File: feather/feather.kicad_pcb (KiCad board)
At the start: 4 copper layers, 61.4 x 38.8 mm, 145 parts, among them CN1 ST-0337D00-071-1A2H, CN2 GT-3321667P-01, J1 Connector, USB-TYPE-C-16P, SW1 1TS015A-1400-0600-CT, SW2 1TS015A-1400-0600-CT, U1 TLV76733DRVx, U10 OPA1622, U11 OPA1622, U2 LM27762, U3 TAD5242IRGER, U4 TLV76733DRVx, U5 OPA1612AxD, U6 RP2350A-QFN60, U7 OPA1612AxD, U8 OPA1612AxD, U9 OPA1622, X1 12MHz

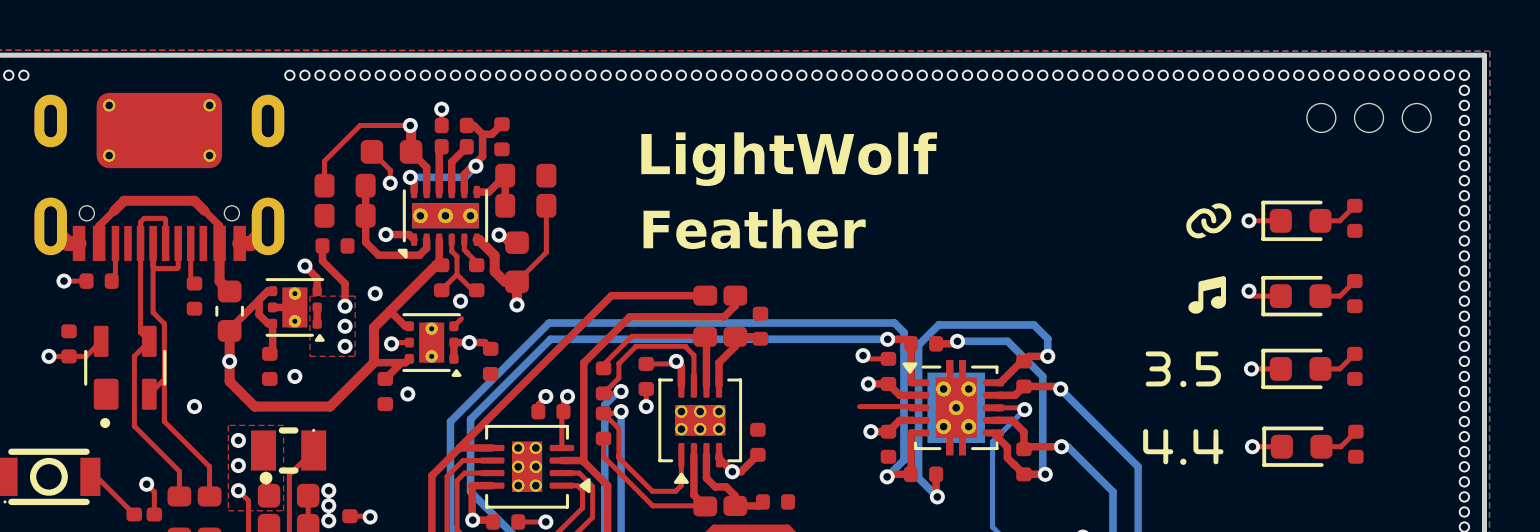
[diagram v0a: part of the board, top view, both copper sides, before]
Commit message: feat: update pcb design and layout
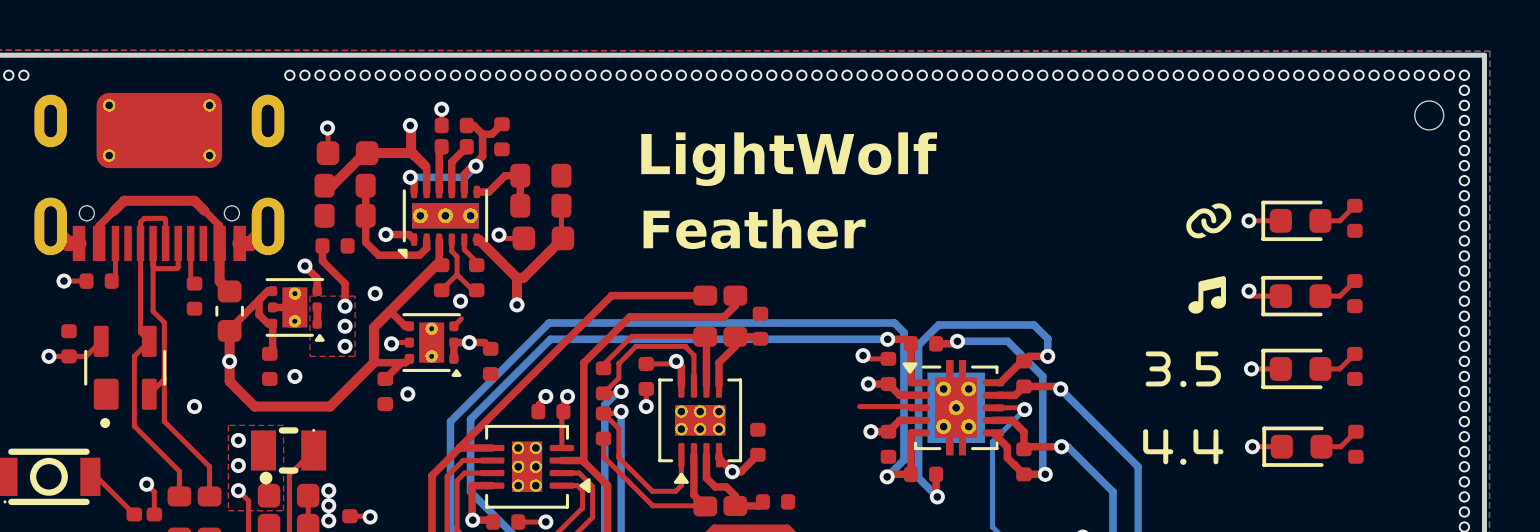
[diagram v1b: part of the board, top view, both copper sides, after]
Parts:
- removed H3, H4: ~, PCM_JLCPCB:Hole_Tooling_JLCPCB
- added G***: LOGO, LOGO, B.Cu at (173.1, 76.0)
- moved C6 1.75 mm to (179.1, 49.9)
- moved G*** 1.60 mm to (217.1, 81.2)
- moved G*** 1.60 mm to (215.1, 81.2)
- moved C20 1.42 mm to (186.9, 53.3), turned to 180 degrees
- moved R6 0.60 mm to (186.8, 50.8)
- moved R9 0.60 mm to (186.8, 52.0)
- moved H2 0.51 mm to (222.2, 48.4)
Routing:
- net +4V5: track 110.6 -> 109.7 mm
- net Net-(U2-FB-): track 2.60 -> 3.20 mm
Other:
- board text added: "TAD5242 DAC OPA1612 op-amp OPA1622 headphone amplifier"

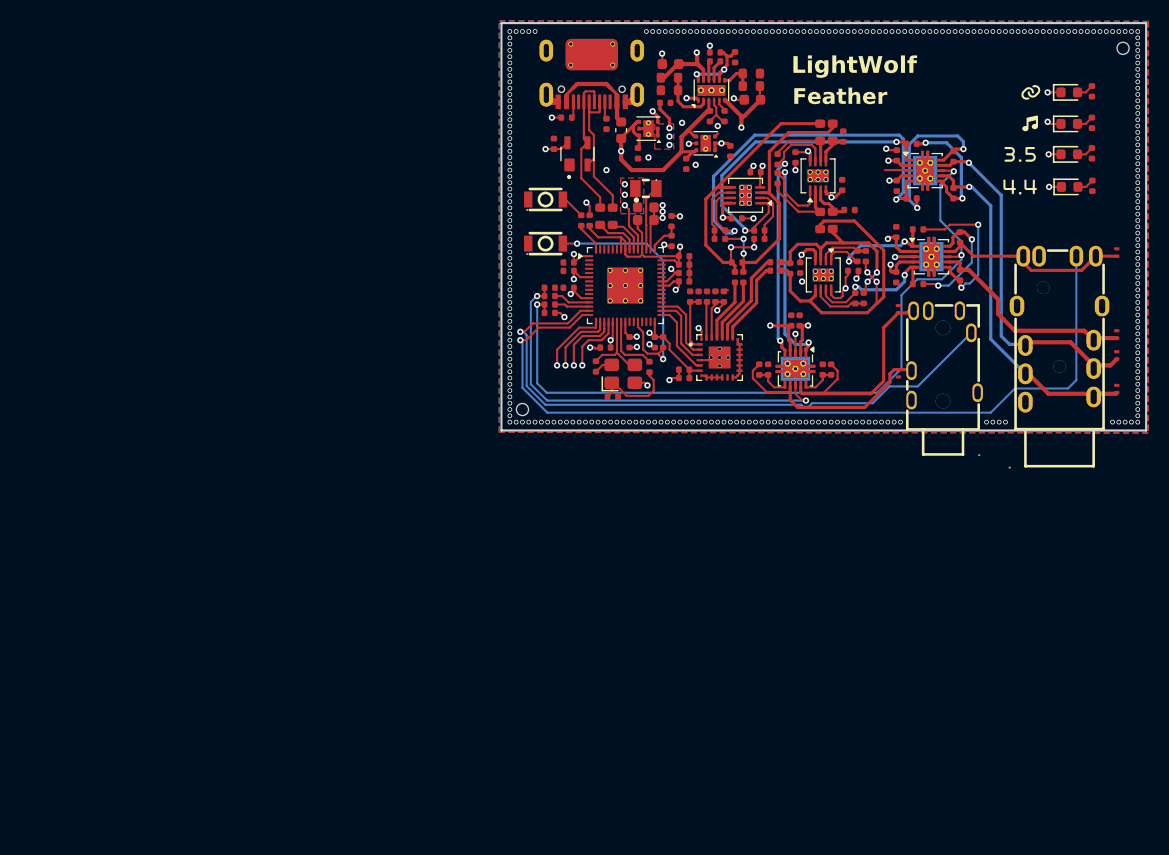
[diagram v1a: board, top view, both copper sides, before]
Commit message: fix: oops forget to connect 3v3 to led
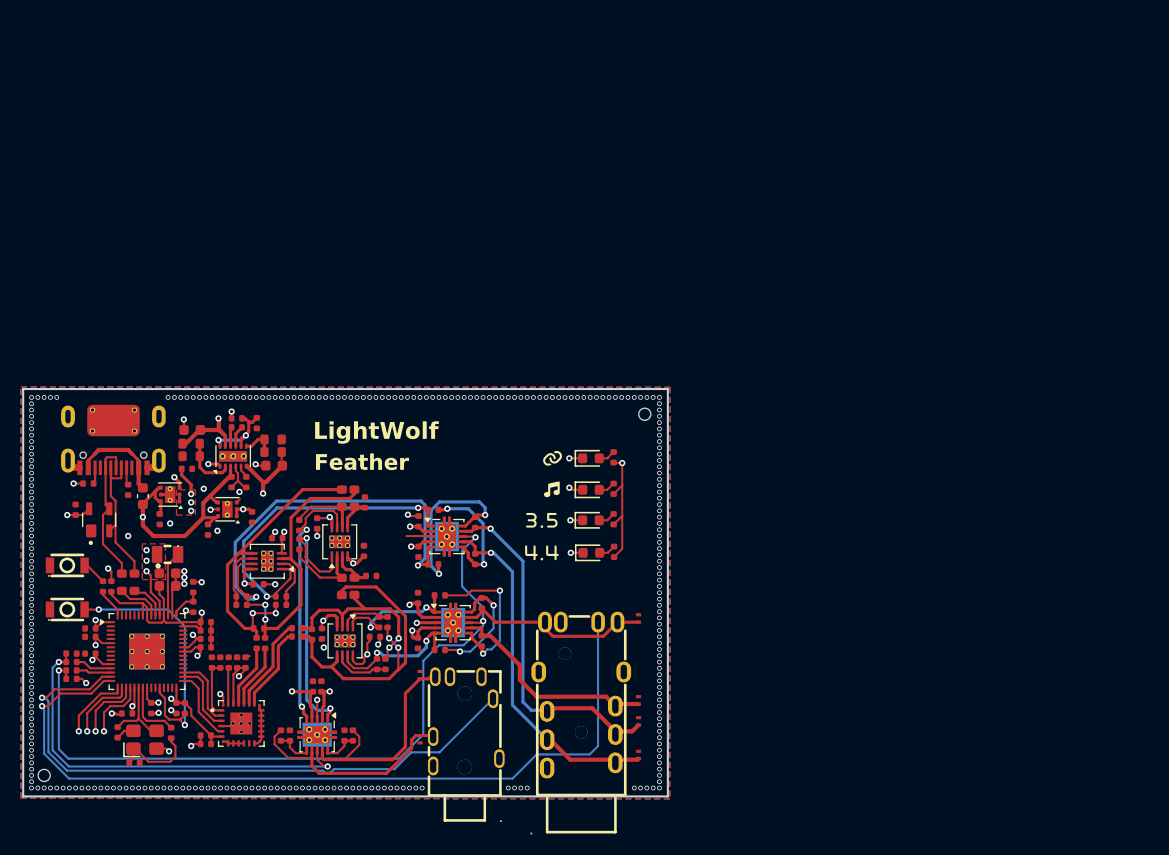
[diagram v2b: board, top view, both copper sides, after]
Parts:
- moved C11 57.4 mm to (138.6, 106.9)
- moved C18 57.4 mm to (139.9, 103.7)
- moved C20 57.4 mm to (141.3, 88.2)
- moved C21 57.4 mm to (123.8, 104.5)
- moved C23 57.4 mm to (134.8, 104.7)
- moved C24 57.4 mm to (125.8, 99.7)
- moved C25 57.4 mm to (123.8, 103.7)
- moved C29 57.4 mm to (134.8, 105.5)
- moved C3 57.4 mm to (134.8, 114.7)
- moved C32 57.4 mm to (145.4, 93.7)
- moved C36 57.4 mm to (131.2, 98.4)
- moved C38 57.4 mm to (150.9, 104.5)
- moved C39 57.4 mm to (139.8, 99.5)
- moved C4 57.4 mm to (130.4, 93.2)
- moved C46 57.4 mm to (155.1, 93.5)
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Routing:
- net +3V3: track 52.8 -> 149.5 mm, vias 10 -> 11

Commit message: feat: update board design
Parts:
- removed the G*** at (167.9, 87.5)
- added G***: LOGO, LOGO, F.Cu at (167.9, 85.0)
- added G***: LOGO, LOGO, F.Cu at (121.6, 101.8)
- added G***: LOGO, LOGO, F.Cu at (121.6, 95.0)
- moved D2 2.45 mm to (171.5, 85.0)
- moved D3 2.45 mm to (171.5, 88.0)
- moved D5 2.45 mm to (171.6, 94.0)
- moved G*** 2.45 mm to (167.8, 88.0)
- moved G*** 2.45 mm to (167.8, 94.0)
- moved G*** 2.45 mm to (165.8, 94.0)
- moved R42 2.45 mm to (173.7, 90.8)
- moved D4 2.45 mm to (171.5, 90.9)
- moved G*** 2.45 mm to (167.8, 90.9)
- moved G*** 2.45 mm to (165.8, 90.9)
- moved R40 2.45 mm to (173.7, 84.9)
- moved R41 2.45 mm to (173.7, 87.9)
- moved R43 2.45 mm to (173.7, 93.9)
- moved SW1 2.25 mm to (121.6, 99.6)
- moved SW2 0.45 mm to (121.6, 97.2)
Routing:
- net /GP14: track 76.6 -> 79.1 mm
- net /GP12: track 72.9 -> 75.4 mm
- net /GP15: track 81.9 -> 84.3 mm
- net /GP13: track 74.1 -> 76.6 mm
- net +3V3: track 149.5 -> 147.0 mm
- net /RUN: track 25.5 -> 27.5 mm
- net GND: track 49.8 -> 48.6 mm
- net Net-(R37-~-Pad1): track 2.37 -> 3.02 mm
